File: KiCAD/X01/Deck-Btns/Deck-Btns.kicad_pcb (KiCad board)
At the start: 2 copper layers, 50 x 100 mm, 45 parts, among them J1 Conn_01x05, J2 Conn_01x05, SW1 SW_Push_LED, SW10 SW_Push_LED, SW2 SW_Push_LED, SW3 SW_Push_LED, SW4 SW_Push_LED, SW5 SW_Push_LED, SW6 SW_Push_LED, SW7 SW_Push_LED, SW8 SW_Push_LED, SW9 SW_Push_LED, U1 CD74HC4067M, U2 74HC595, U3 74HC595

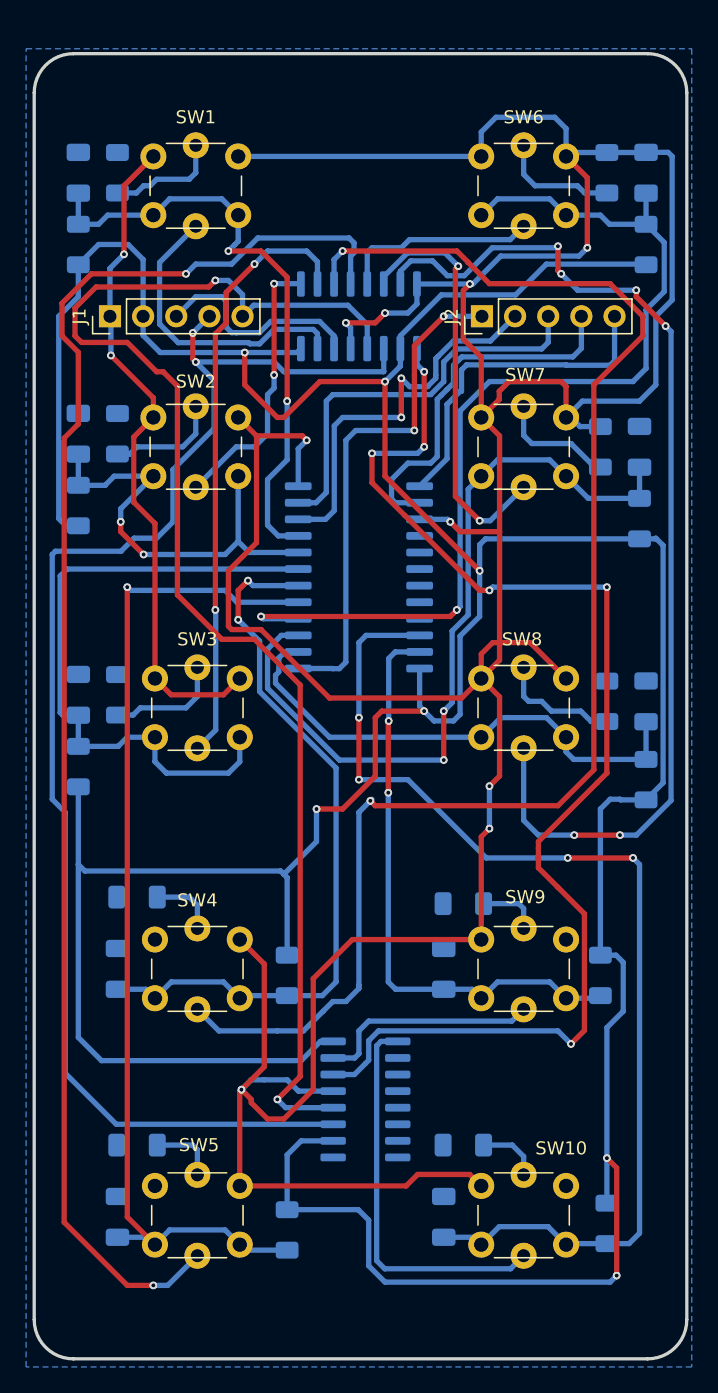
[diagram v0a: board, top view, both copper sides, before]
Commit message: deck btns fixes
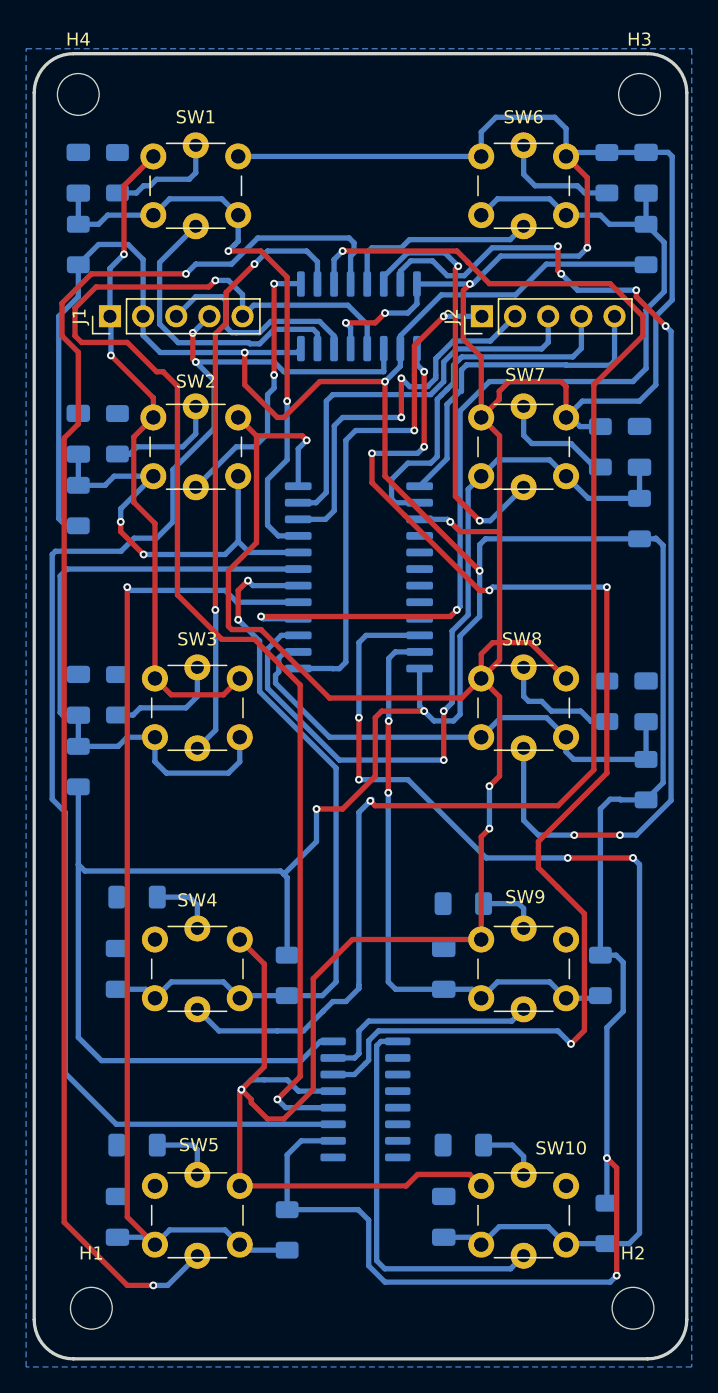
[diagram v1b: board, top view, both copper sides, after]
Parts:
- added H1: MountingHole, MountingHole:MountingHole_3.2mm_M3, F.Cu at (74.5, 131.0)
- added H2: MountingHole, MountingHole:MountingHole_3.2mm_M3, F.Cu at (116.0, 131.0)
- added H3: MountingHole, MountingHole:MountingHole_3.2mm_M3, F.Cu at (116.5, 38.0)
- added H4: MountingHole, MountingHole:MountingHole_3.2mm_M3, F.Cu at (73.5, 38.0)

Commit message: dck btns
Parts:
- removed C1, C10, C2, C3, C4, C5, C6, C7, C8, C9: 1uF, Capacitor_SMD:C_1206_3216Metric_Pad1.33x1.80mm_HandSolder
- removed J2: Conn_01x05, Connector_PinHeader_2.54mm:PinHeader_1x05_P2.54mm_Vertical
- removed R10, R16, R17, R18, R19, R20, R5, R6, R7, R8: 10K, PCM_Resistor_SMD_AKL:R_1206_3216Metric_Pad1.30x1.75mm_HandSolder
- removed R11, R12, R13, R14, R15, R3, R4, R9: 220, PCM_Resistor_SMD_AKL:R_1206_3216Metric_Pad1.30x1.75mm_HandSolder
- removed U2, U3: 74HC595, Package_SO:SOIC-16_3.9x9.9mm_P1.27mm
- added D1: 1N4148, Diode_SMD:D_SOD-123, B.Cu at (109.5, 75.0)
- added D10: 1N4148, Diode_SMD:D_SOD-123, B.Cu at (101.5, 63.5)
- added D11: 1N4148, Diode_SMD:D_SOD-123, B.Cu at (102.5, 83.0)
- added D12: 1N4148, Diode_SMD:D_SOD-123, B.Cu at (102.0, 103.0)
- added D13: 1N4148, Diode_SMD:D_SOD-123, B.Cu at (102.5, 122.0)
- added D2: 1N4148, Diode_SMD:D_SOD-123, B.Cu at (76.5, 46.5)
- added D3: 1N4148, Diode_SMD:D_SOD-123, B.Cu at (77.0, 67.0)
- added D4: 1N4148, Diode_SMD:D_SOD-123, B.Cu at (76.5, 87.0)
- added D5: 1N4148, Diode_SMD:D_SOD-123, B.Cu at (77.0, 107.0)
- added D6: 1N4148, Diode_SMD:D_SOD-123, B.Cu at (77.0, 125.0)
- added D7: 1N4148, Diode_SMD:D_SOD-123, B.Cu at (85.5, 77.5)
- added D8: 1N4148, Diode_SMD:D_SOD-123, B.Cu at (85.5, 75.0)
- added D9: 1N4148, Diode_SMD:D_SOD-123, B.Cu at (106.6, 53.2)
- added JP1: A0, Jumper:SolderJumper-2_P1.3mm_Open_RoundedPad1.0x1.5mm, B.Cu at (105.5, 73.5)
- added JP2: A1, Jumper:SolderJumper-2_P1.3mm_Open_RoundedPad1.0x1.5mm, B.Cu at (105.5, 77.0)
- R1, R2: value 220 -> 47K; footprint PCM_Resistor_SMD_AKL:R_1206_3216Metric_Pad1.30x1.75mm_HandSolder -> Resistor_SMD:R_0805_2012Metric_Pad1.20x1.40mm_HandSolder
- SW1: value SW_Push_LED -> DECK-SW1; footprint led-switch:SW_PUSH_6mm_LED -> led-sw:led switch
- SW10: value SW_Push_LED -> DECK-SW10; footprint led-switch:SW_PUSH_6mm_LED -> led-sw:led switch
- SW2: value SW_Push_LED -> DECK-SW2; footprint led-switch:SW_PUSH_6mm_LED -> led-sw:led switch
- SW3: value SW_Push_LED -> DECK-SW3; footprint led-switch:SW_PUSH_6mm_LED -> led-sw:led switch
- SW4: value SW_Push_LED -> DECK-SW4; footprint led-switch:SW_PUSH_6mm_LED -> led-sw:led switch
- SW5: value SW_Push_LED -> DECK-SW5; footprint led-switch:SW_PUSH_6mm_LED -> led-sw:led switch
- SW6: value SW_Push_LED -> DECK-SW6; footprint led-switch:SW_PUSH_6mm_LED -> led-sw:led switch
- SW7: value SW_Push_LED -> DECK-SW7; footprint led-switch:SW_PUSH_6mm_LED -> led-sw:led switch
- SW8: value SW_Push_LED -> DECK-SW8; footprint led-switch:SW_PUSH_6mm_LED -> led-sw:led switch
- SW9: value SW_Push_LED -> DECK-SW9; footprint led-switch:SW_PUSH_6mm_LED -> led-sw:led switch
- U1: value CD74HC4067M -> HT16K33 24SOP; footprint Package_SO:SOIC-24W_7.5x15.4mm_P1.27mm -> Package_SO:SSOP-24_5.3x8.2mm_P0.65mm
- moved R1 44.0 mm to (110.0, 72.5), turned to 0 degrees
- moved R2 36.1 mm to (110.0, 77.5), turned to 0 degrees
- moved J1 24.1 mm to (100.0, 54.0), turned to -90 degrees
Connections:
- net +5V renamed VCC
- J1 pad 3: DECK-LED-SIG -> /SCL
- J1 pad 4: SRCLK -> /SCA
- J1 pad 5: DECK-LED-LATCH -> /INT
- R1 pad 1: GND -> Net-(JP1-B)
- R1 pad 2: Net-(SW1-K) -> Net-(D1-K)
- R2 pad 1: GND -> Net-(JP2-B)
- R2 pad 2: Net-(SW2-K) -> Net-(D1-K)
- SW1 pad 1: GND -> /KS-1
- SW1 pad 2: DECK-SW1 -> Net-(D2-A)
- SW1 pad 3: Net-(SW1-K) -> /COM-0
- SW1 pad 4: DECK-LED-1 -> /R2
- SW10 pad 1: GND -> /KS-2
- SW10 pad 2: DECK-SW10 -> Net-(D13-A)
- SW10 pad 3: Net-(SW10-K) -> /COM-1
- SW10 pad 4: DECK-LED-10 -> /R6
- SW2 pad 1: GND -> /KS-1
- SW2 pad 2: DECK-SW2 -> Net-(D3-A)
- SW2 pad 3: Net-(SW2-K) -> /COM-0
- SW2 pad 4: DECK-LED-2 -> /R3
- SW3 pad 1: GND -> /KS-1
- SW3 pad 2: DECK-SW3 -> Net-(D4-A)
- SW3 pad 3: Net-(SW3-K) -> /COM-0
- SW3 pad 4: DECK-LED-3 -> /R4
- SW4 pad 1: GND -> /KS-1
- SW4 pad 2: DECK-SW4 -> Net-(D5-A)
- SW4 pad 3: Net-(SW4-K) -> /COM-0
- SW4 pad 4: DECK-LED-4 -> /R5
- SW5 pad 1: GND -> /KS-1
- SW5 pad 2: DECK-SW5 -> Net-(D6-A)
- SW5 pad 3: Net-(SW5-K) -> /COM-0
- SW5 pad 4: DECK-LED-5 -> /R6
- SW6 pad 1: GND -> /KS-2
- SW6 pad 2: DECK-SW6 -> Net-(D9-A)
- SW6 pad 3: Net-(SW6-K) -> /COM-1
- SW6 pad 4: DECK-LED-6 -> /R2
- SW7 pad 1: GND -> /KS-2
- SW7 pad 2: DECK-SW7 -> Net-(D10-A)
- SW7 pad 3: Net-(SW7-K) -> /COM-1
- SW7 pad 4: DECK-LED-7 -> /R3
- SW8 pad 1: GND -> /KS-2
- SW8 pad 2: DECK-SW8 -> Net-(D11-A)
- SW8 pad 3: Net-(SW8-K) -> /COM-1
- SW8 pad 4: DECK-LED-8 -> /R4
- SW9 pad 1: GND -> /KS-2
- SW9 pad 2: DECK-SW9 -> Net-(D12-A)
- SW9 pad 3: Net-(SW9-K) -> /COM-1
- SW9 pad 4: DECK-LED-9 -> /R5
- U1 pad 1: MPLEX-DECK -> GND
- U1 pad 10: MPLEX-S0 -> /INT
- U1 pad 11: MPLEX-S1 -> unconnected-(U1-ROW10/K9-Pad11)
- U1 pad 12: GND -> unconnected-(U1-ROW9/K8-Pad12)
- U1 pad 13: MPLEX-S3 -> unconnected-(U1-ROW8/K7-Pad13)
- U1 pad 14: MPLEX-S2 -> unconnected-(U1-ROW7/K6-Pad14)
- U1 pad 15: GND -> /R6
- U1 pad 16: unconnected-(U1-I15-Pad16) -> /R5
- U1 pad 17: unconnected-(U1-I14-Pad17) -> /R4
- U1 pad 18: unconnected-(U1-I13-Pad18) -> /R3
- U1 pad 19: unconnected-(U1-I12-Pad19) -> /R2
- U1 pad 2: DECK-SW8 -> /COM-0
- U1 pad 20: unconnected-(U1-I11-Pad20) -> /R1
- U1 pad 21: unconnected-(U1-I10-Pad21) -> /R0
- U1 pad 22: DECK-SW10 -> /SCL
- U1 pad 23: DECK-SW9 -> /SCA
- U1 pad 3: DECK-SW7 -> /COM-1
- U1 pad 4: DECK-SW6 -> /COM-2
- U1 pad 5: DECK-SW5 -> /COM-3
- U1 pad 6: DECK-SW4 -> unconnected-(U1-COM4-Pad6)
- U1 pad 7: DECK-SW3 -> unconnected-(U1-COM5-Pad7)
- U1 pad 8: DECK-SW2 -> unconnected-(U1-COM6-Pad8)
- U1 pad 9: DECK-SW1 -> unconnected-(U1-COM7-Pad9)
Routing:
- net GND: track 355.6 -> 5.27 mm, vias 11 -> 2
- net VCC: track 325.0 -> 3.61 mm, vias 7 -> 1
- net /COM-0: track 0.00 -> 137.8 mm, vias 0 -> 6
- net /KS-2: track 0.00 -> 125.9 mm, vias 0 -> 1
- net DECK-LED-5: track 112.4 -> 0.00 mm, vias 2 -> 0
- net /COM-1: track 0.00 -> 111.9 mm, vias 0 -> 2
- net DECK-LED-4: track 111.9 -> 0.00 mm, vias 2 -> 0
- net SRCLK: track 107.3 -> 0.00 mm, vias 2 -> 0
- net DECK-LED-LATCH: track 105.0 -> 0.00 mm, vias 2 -> 0
- net Net-(U2-QH'): track 95.7 -> 0.00 mm, vias 6 -> 0
- net /KS-1: track 0.00 -> 92.8 mm
- net /R6: track 0.00 -> 89.2 mm, vias 0 -> 2
- net DECK-SW10: track 84.6 -> 0.00 mm, vias 4 -> 0
- net DECK-LED-8: track 81.9 -> 0.00 mm, vias 6 -> 0
- net DECK-SW5: track 79.2 -> 0.00 mm, vias 1 -> 0
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- added copper zone on F.Cu, net VCC
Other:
- board text added: "GND"
- board text added: "INT"
- board text added: "SCA"
- board text added: "SCL"
- board text added: "VCC"
